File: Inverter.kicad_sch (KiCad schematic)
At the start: 44 parts, among them Q2 BSC022N04LSATMA1, Q3 BSC022N04LSATMA1, Q4 BSC022N04LSATMA1, Q5 BSC022N04LSATMA1, Q6 BSC022N04LSATMA1, Q7 BSC022N04LSATMA1, U4 TMC6140, U5 TSC2011, U6 TSC2011

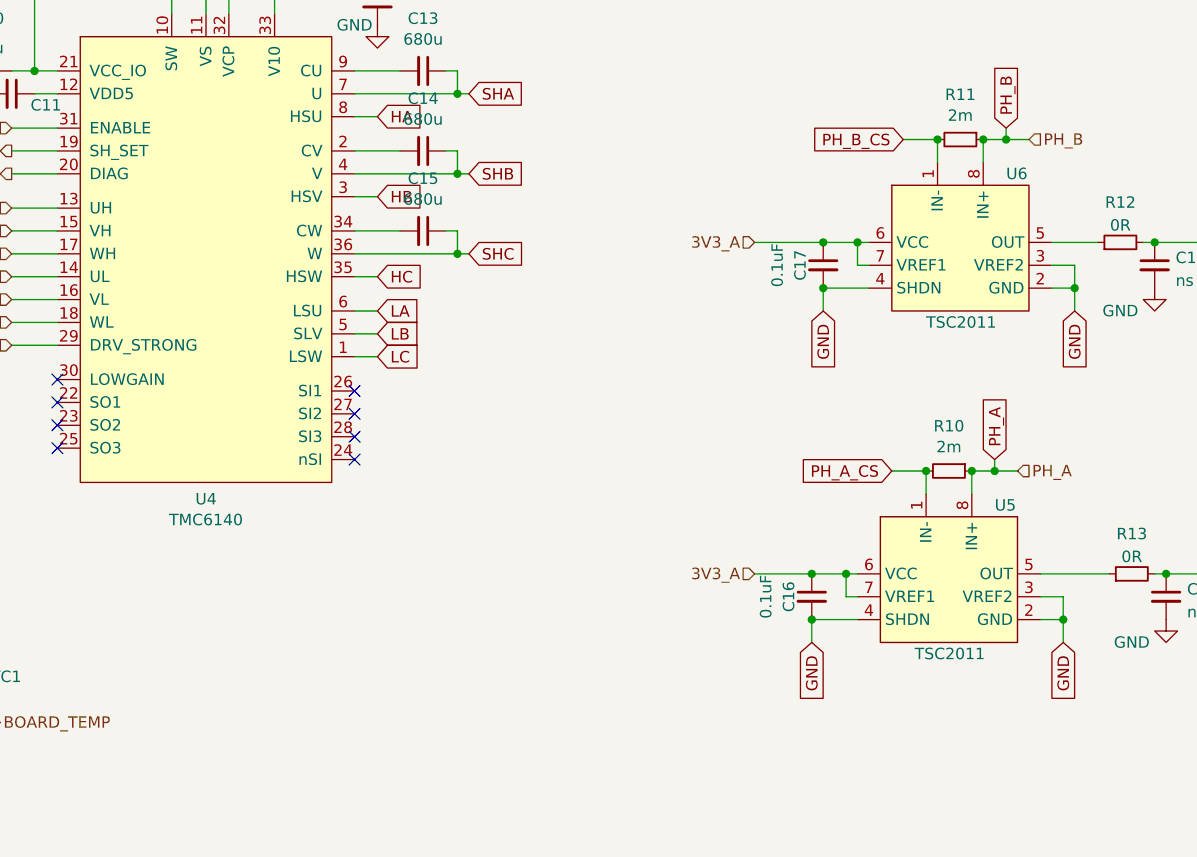
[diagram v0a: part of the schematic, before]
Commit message: added local symbol library
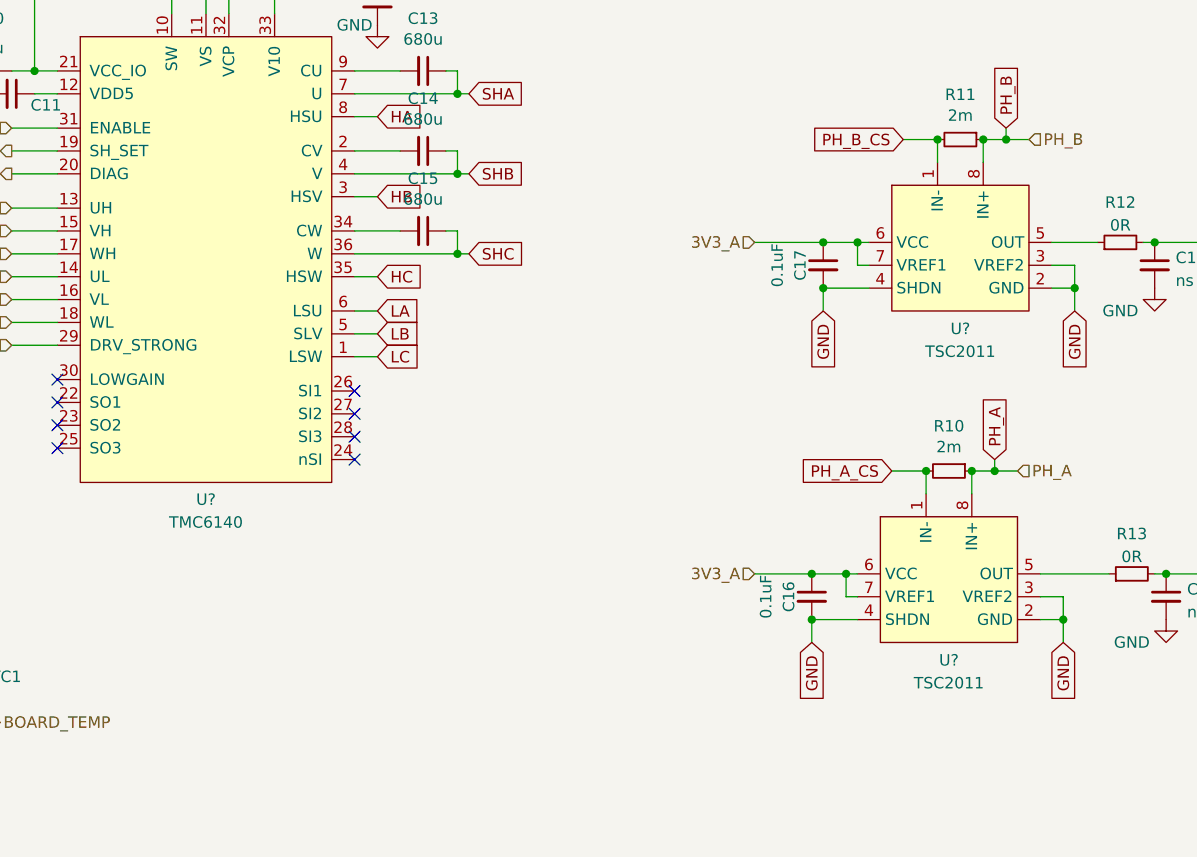
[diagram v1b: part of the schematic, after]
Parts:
- removed U4: TMC6140, symbol MyLibrary:TMC6140
- removed U5, U6: TSC2011, symbol Mylibrary:TSC2011
- added U? (x2): TSC2011, symbol MyLibrary_PMSM:TSC2011
- added U?: TMC6140, symbol MyLibrary_PMSM:TMC6140
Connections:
- net 3.3v: now also U?.21 (VCC_IO)
- net 3V3_A: now also U?.6 (VCC), U?.6 (VCC), U?.7 (VREF1), U?.7 (VREF1)
- net DIAG: now also U?.20 (DIAG)
- net DRV_STRONG: now also U?.29 (DRV_STRONG)
- net ENABLE: now also U?.31 (ENABLE)
- net GND: now also U?.2 (GND), U?.2 (GND), U?.3 (VREF2), U?.3 (VREF2), U?.4 (SHDN), U?.4 (SHDN)
- net HA: now also U?.8 (HSU)
- net HB: now also U?.3 (HSV)
- net HC: now also U?.35 (HSW)
- net LA: now also U?.6 (LSU)
- net LB: now also U?.5 (SLV)
- net LC: now also U?.1 (LSW)
- net PH_A: now also U?.8 (IN+)
- net PH_A_CS: now also U?.1 (IN-), U?.7 (U)
- net PH_B: now also U?.8 (IN+)
- net PH_B_CS: now also U?.1 (IN-), U?.4 (V)
- net PH_C: now also U?.36 (W)
- net PWM_HA: now also U?.13 (UH)
- net PWM_HB: now also U?.15 (VH)
- net PWM_HC: now also U?.17 (WH)
- net PWM_LA: now also U?.14 (UL)
- net PWM_LB: now also U?.16 (VL)
- net PWM_LC: now also U?.18 (WL)
- net SH_SET: now also U?.19 (SH_SET)
- net VDD: now also U?.11 (VS), U?.32 (VCP)
- net at C13.2: now also U?.9 (CU)
- net at C14.2: now also U?.2 (CV)
- net at C15.2: now also U?.34 (CW)
- net at 68u1.2: now also U?.10 (SW)
- net at C11.1: now also U?.12 (VDD5)
- net at C12.1: now also U?.33 (V10)
- net at R13.1: now also U?.5 (OUT)
- net at R12.1: now also U?.5 (OUT)

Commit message: Third commit
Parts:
- U4: renamed from U?; footprint (none) -> MyLibrary:TMC6140-LA
- gave numbers to parts that had none: 2
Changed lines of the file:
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@@
   (symbol (lib_id "MyLibrary_PMSM:TSC2011") (at 151.13 138.43 0) (unit 1)
     (in_bom yes) (on_board yes) (fields_autoplaced)
-    (property "Reference" "U?" (id 0) (at 151.13 150.5696 0))
+    (property "Reference" "U5" (id 0) (at 151.13 150.5696 0))
     (property "Value" "TSC2011" (id 1) (at 151.13 153.1065 0))
     (property "Footprint" "" (id 2) (at 151.13 138.43 0)
@@
   (symbol (lib_id "MyLibrary_PMSM:TMC6140") (at 68.58 105.41 0) (unit 1)
     (in_bom yes) (on_board yes) (fields_autoplaced)
-    (property "Reference" "U?" (id 0) (at 68.58 132.7134 0))
+    (property "Reference" "U4" (id 0) (at 68.58 132.7134 0))
     (property "Value" "TMC6140" (id 1) (at 68.58 135.2503 0))
-    (property "Footprint" "" (id 2) (at 83.82 93.98 0)
+    (property "Footprint" "MyLibrary:TMC6140-LA" (id 2) (at 83.82 93.98 0)
       (effects (font (size 1.27 1.27)) hide)
     )
@@
   (symbol (lib_id "MyLibrary_PMSM:TSC2011") (at 152.4 101.6 0) (unit 1)
     (in_bom yes) (on_board yes) (fields_autoplaced)
-    (property "Reference" "U?" (id 0) (at 152.4 113.7396 0))
+    (property "Reference" "U6" (id 0) (at 152.4 113.7396 0))
     (property "Value" "TSC2011" (id 1) (at 152.4 116.2765 0))
     (property "Footprint" "" (id 2) (at 152.4 101.6 0)

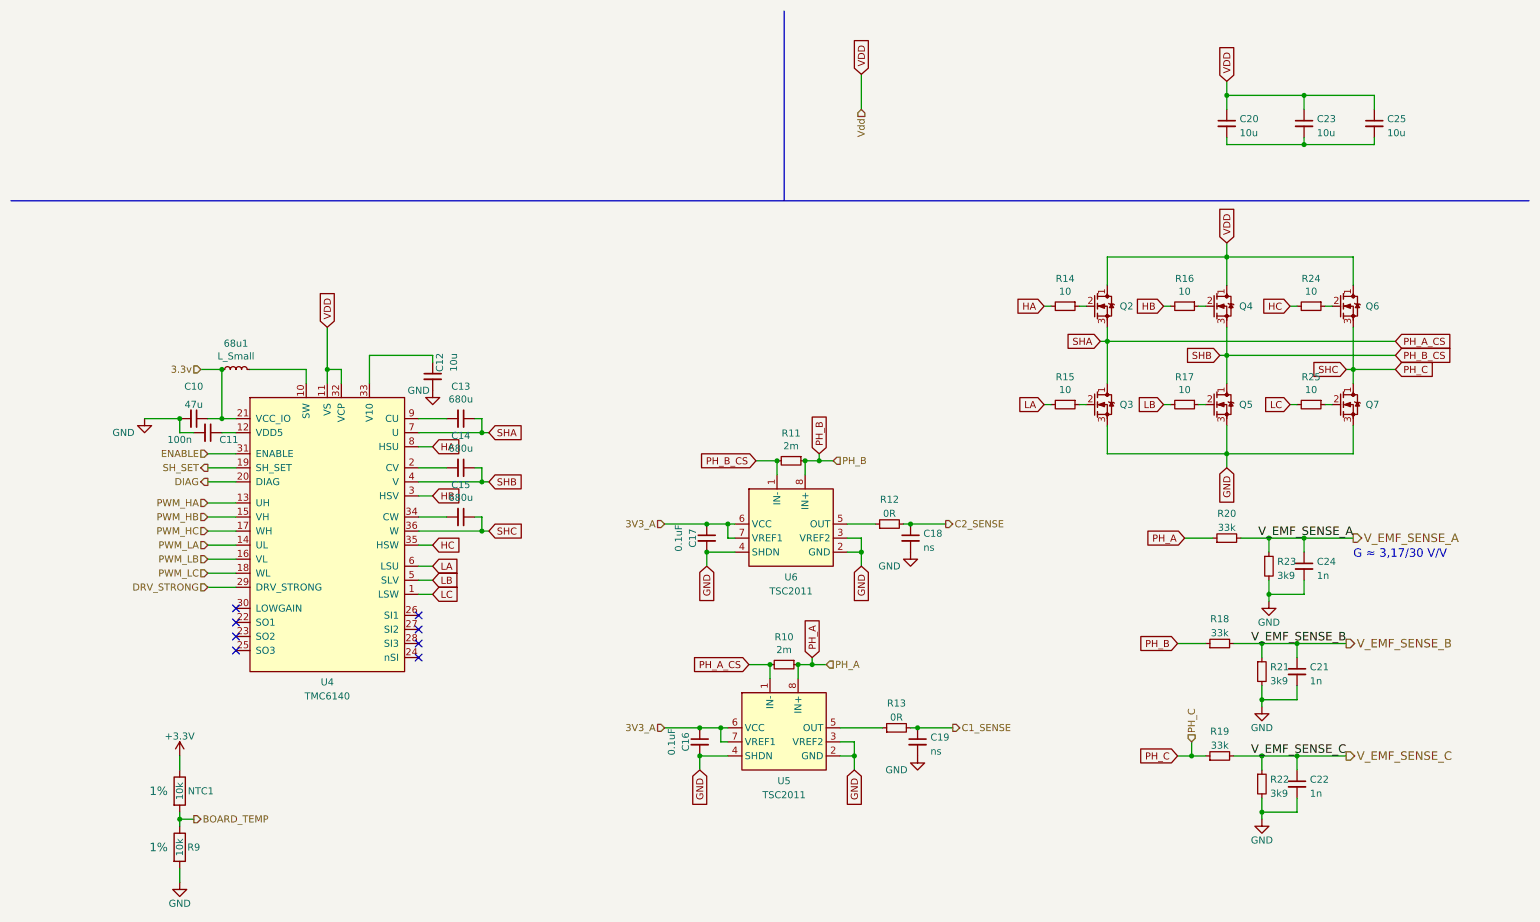
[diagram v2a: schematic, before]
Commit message: added footprints
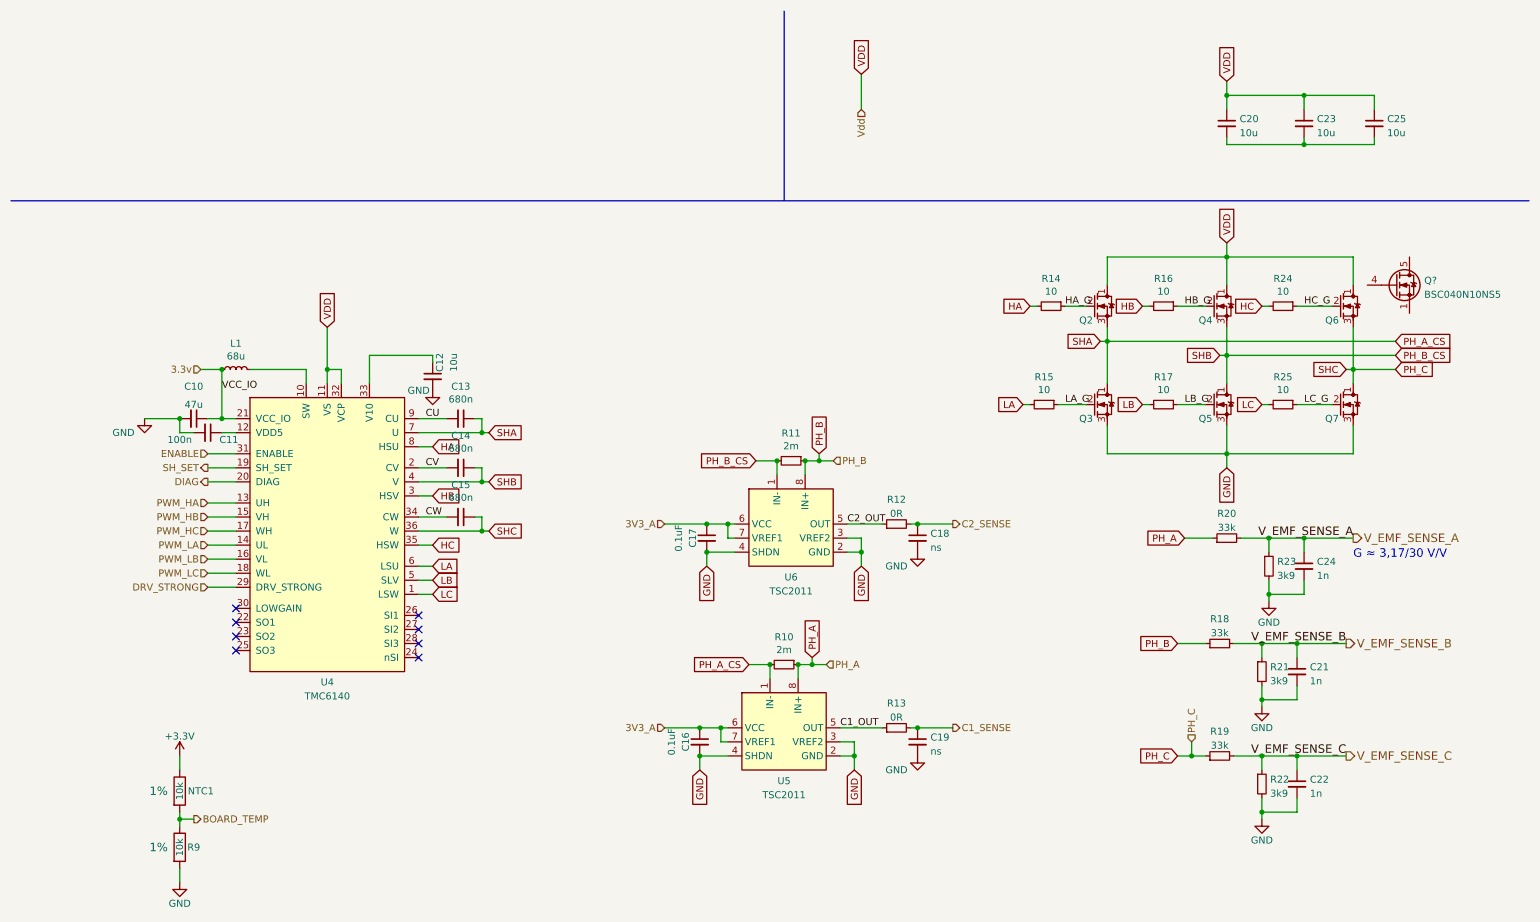
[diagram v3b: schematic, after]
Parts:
- added Q?: BSC040N10NS5, Package_TO_SOT_SMD:TDSON-8-1, symbol Transistor_FET:BSC040N10NS5
- C10: footprint (none) -> Capacitor_SMD:C_1206_3216Metric
- C11, C12, C18, C19, C20, C21, C22, C23, C24, C25: footprint (none) -> Capacitor_SMD:C_0603_1608Metric
- C13, C14, C15: value 680u -> 680n; footprint (none) -> Capacitor_SMD:C_0603_1608Metric
- L1: renamed from 68u1; value L_Small -> 68u; footprint (none) -> Inductor_SMD:L_Sunlord_MWSA0518_5.4x5.2mm
- Q2, Q3, Q4, Q5, Q6, Q7: footprint (none) -> MyLibrary:TDSON-8-6
- R10, R11: footprint (none) -> Resistor_SMD:R_2512_6332Metric
- R12, R13, R14, R15, R16, R17, R18, R19, R20, R21, R22, R23, R24, R25: footprint (none) -> Resistor_SMD:R_0603_1608Metric
- U5, U6: footprint (none) -> Package_SO:SOIC-8_3.9x4.9mm_P1.27mm
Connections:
- net HA_G: now reaches Q2.2 (G), R14.1
- net LA_G: now reaches Q3.2 (G), R15.1
- net HB_G: now reaches Q4.2 (G), R16.1
- net LB_G: now reaches Q5.2 (G), R17.1
- net HC_G: now reaches Q6.2 (G), R24.1
- net LC_G: now reaches Q7.2 (G), R25.1
- net CU: now reaches C13.2, U4.9 (CU)
- net CV: now reaches C14.2, U4.2 (CV)
- net CW: now reaches C15.2, U4.34 (CW)
- net C1_OUT: now reaches R13.1, U5.5 (OUT)
- net C2_OUT: now reaches R12.1, U6.5 (OUT)
- new net: Q?.1 (S), Q?.2 (S), Q?.3 (S)
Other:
- moved on the sheet: C18, R12, R14, R15, R16, R17, R24, R25

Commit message: fourth commit
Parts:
- Q2, Q3, Q4, Q5, Q6, Q7: footprint MyLibrary:TDSON-8-6 -> MyLibrary:TDSON-8-6_copy
- gave numbers to parts that had none: 1
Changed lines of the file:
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@@
       (effects (font (size 1.27 1.27)) (justify left) hide)
     )
-    (property "Footprint" "MyLibrary:TDSON-8-6" (id 2) (at 212.09 62.23 0)
+    (property "Footprint" "MyLibrary:TDSON-8-6_copy" (id 2) (at 212.09 62.23 0)
       (effects (font (size 1.27 1.27)) hide)
     )
@@
       (effects (font (size 1.27 1.27)) (justify left) hide)
     )
-    (property "Footprint" "MyLibrary:TDSON-8-6" (id 2) (at 212.09 80.01 0)
+    (property "Footprint" "MyLibrary:TDSON-8-6_copy" (id 2) (at 212.09 80.01 0)
       (effects (font (size 1.27 1.27)) hide)
     )
@@
       (effects (font (size 1.27 1.27)) (justify left) hide)
     )
-    (property "Footprint" "MyLibrary:TDSON-8-6" (id 2) (at 233.68 62.23 0)
+    (property "Footprint" "MyLibrary:TDSON-8-6_copy" (id 2) (at 233.68 62.23 0)
       (effects (font (size 1.27 1.27)) hide)
     )
@@
       (effects (font (size 1.27 1.27)) (justify left) hide)
     )
-    (property "Footprint" "MyLibrary:TDSON-8-6" (id 2) (at 233.68 80.01 0)
+    (property "Footprint" "MyLibrary:TDSON-8-6_copy" (id 2) (at 233.68 80.01 0)
       (effects (font (size 1.27 1.27)) hide)
     )
@@
       (effects (font (size 1.27 1.27)) (justify left) hide)
     )
-    (property "Footprint" "MyLibrary:TDSON-8-6" (id 2) (at 256.54 62.23 0)
+    (property "Footprint" "MyLibrary:TDSON-8-6_copy" (id 2) (at 256.54 62.23 0)
       (effects (font (size 1.27 1.27)) hide)
     )
@@
       (effects (font (size 1.27 1.27)) (justify left) hide)
     )
-    (property "Footprint" "MyLibrary:TDSON-8-6" (id 2) (at 256.54 80.01 0)
+    (property "Footprint" "MyLibrary:TDSON-8-6_copy" (id 2) (at 256.54 80.01 0)
       (effects (font (size 1.27 1.27)) hide)
     )
@@
   (symbol (lib_id "Transistor_FET:BSC040N10NS5") (at 261.62 60.96 0) (unit 1)
     (in_bom yes) (on_board yes) (fields_autoplaced)
-    (property "Reference" "Q?" (id 0) (at 266.827 60.1253 0)
-      (effects (font (size 1.27 1.27)) (justify left))
-    )
+    (property "Reference" "Q9" (id 0) (at 266.827 60.1253 0)
+      (effects (font (size 1.27 1.27)) (justify left))
+    )

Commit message: rev_0.1
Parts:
- removed Q9: BSC040N10NS5, Package_TO_SOT_SMD:TDSON-8-1, symbol Transistor_FET:BSC040N10NS5
- added C38: 22u, Capacitor_SMD:C_0603_1608Metric, symbol Device:C_Small
- C10: value 47u -> 22u; footprint Capacitor_SMD:C_1206_3216Metric -> Capacitor_SMD:C_0603_1608Metric
- L1: footprint Inductor_SMD:L_Sunlord_MWSA0518_5.4x5.2mm -> Inductor_SMD:L_1210_3225Metric
- NTC1: footprint Resistors_SMD:R_0603 -> Resistor_SMD:R_0603_1608Metric
- R9: footprint Resistors_SMD:R_0402 -> Resistor_SMD:R_0603_1608Metric
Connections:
- net 3.3v: now also C38.1
- net GND: now also C20.2, C23.2, C25.2, C38.2
- net HA: now also R16.2; no longer R14.2
- net HA_G: now also Q4.2 (G), R16.1; no longer Q2.2 (G), R14.1
- net HB: now also R24.2; no longer R16.2
- net HB_G: now also Q6.2 (G), R24.1; no longer Q4.2 (G), R16.1
- net HC: now also R14.2; no longer R24.2
- net HC_G: now also Q2.2 (G), R14.1; no longer Q6.2 (G), R24.1
- net LA: now also R17.2; no longer R15.2
- net LA_G: now also Q5.2 (G), R17.1; no longer Q3.2 (G), R15.1
- net LB: now also R25.2; no longer R17.2
- net LB_G: now also Q7.2 (G), R25.1; no longer Q5.2 (G), R17.1
- net LC: now also R15.2; no longer R25.2
- net LC_G: now also Q3.2 (G), R15.1; no longer Q7.2 (G), R25.1
- net PH_A: now also R11.1, U6.8 (IN+); no longer R10.1, R20.1, U5.8 (IN+)
- net PH_A_CS: now also Q4.3 (S), Q5.1 (D), R11.2, R19.1, U6.1 (IN-); no longer Q2.3 (S), Q3.1 (D), R10.2, U5.1 (IN-)
- net PH_B: now also C14.1, Q6.3 (S), Q7.1 (D), U4.4 (V); no longer R11.1, U6.8 (IN+)
- net PH_C: now also R10.1, U5.8 (IN+); no longer C15.1, Q6.3 (S), Q7.1 (D), R19.1, U4.36 (W)
- net V_EMF_SENSE_A: now also C22.1, R19.2, R22.1; no longer C24.1, R20.2, R23.1
- net V_EMF_SENSE_C: now also C24.1, R20.2, R23.1; no longer C22.1, R19.2, R22.1
- net SW: now reaches L1.2, U4.10 (SW)
- net V10: now reaches C12.1, U4.33 (V10)
- removed net PH_B_CS: C14.1, Q4.3 (S), Q5.1 (D), R11.2, U4.4 (V), U6.1 (IN-)
- new net PH_C_CS: C15.1, Q2.3 (S), Q3.1 (D), R10.2, R20.1, U4.36 (W), U5.1 (IN-)
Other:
- moved on the sheet: L1

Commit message: layout
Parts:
- added R35, R36, R6: 3k9, Resistor_SMD:R_0603_1608Metric, symbol Device:R_Small
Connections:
- net V_EMF_SENSE_A: now also R6.2; no longer R19.2, R22.1
- net V_EMF_SENSE_B: now also R35.2; no longer R18.2, R21.1
- net V_EMF_SENSE_C: now also R36.2; no longer R20.2, R23.1
- new net V_EMF_SENSE_A_NF: R19.2, R22.1, R6.1
- new net V_EMF_SENSE_B_NF: R18.2, R21.1, R35.1
- new net V_EMF_SENSE_C_NF: R20.2, R23.1, R36.1
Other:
- moved on the sheet: C21, C22, R18, R19, R20, R21, R22, R23

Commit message: before load switch
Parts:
- added D3, D7, D8: D_Zener_Small, Diode_SMD:D_SOD-123, symbol Device:D_Zener_Small
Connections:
- net GND: now also D3.2 (A), D7.2 (A), D8.2 (A)
- net V_EMF_SENSE_A: now also D3.1 (K)
- net V_EMF_SENSE_B: now also D7.1 (K)
- net V_EMF_SENSE_C: now also D8.1 (K)

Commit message: final
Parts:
- added C44, C45: 220n, Capacitor_SMD:C_0603_1608Metric, symbol Device:C_Small
- added C49, C50, C51: 1n, Capacitor_SMD:C_0603_1608Metric, symbol Device:C_Small
- added TP11, TP12, TP13, TP19, TP2, TP3, TP4, TP5, TP6, TP7, TP8, TP9: TestPoint, MyLibrary:TestPoint_1.0mm, symbol Connector:TestPoint
- added TP20, TP21, TP22, TP23, TP24, TP25, TP26, TP27: Testpoint, MyLibrary:TestPoint_1.0mm, symbol Connector:TestPoint
- C10, C38: Part (none) -> CL10A226MQ8NRNC
- C11: footprint Capacitor_SMD:C_0603_1608Metric -> Capacitor_SMD:C_0402_1005Metric; Part (none) -> CL05B104KA5NNNC
- C12: Part (none) -> CL21A106KOQNNNG
- C13, C14, C15: value 680n -> 1u; Part (none) -> CL10B105KA8NNNC
- C16, C17: value 0.1uF -> 100n; Part (none) -> CL05B104KA5NNNC
- C20, C23, C25: footprint Capacitor_SMD:C_0603_1608Metric -> Capacitor_SMD:C_1206_3216Metric; Part (none) -> CL31B106KBHNNNE
- C21, C22, C24: Part (none) -> CL10B102KB8NNNC
- D3, D7, D8: Part (none) -> MMSZ5231B-7-F
- L1: Part (none) -> CBC3225T680KR
- NTC1: Part (none) -> NCU18XH103F60RB
- Q2, Q3, Q4, Q5, Q6, Q7: Part (none) -> BSC022N04LSATMA1 ------
- R10, R11: Part (none) -> gia prese
- R14, R15, R16, R17, R24, R25: value 10 -> 2.2
- U4: Part (none) -> TMC6140 ---------
- U5, U6: Part (none) -> TSC2011 ----
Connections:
- net BOARD_TEMP: now also TP19.1
- net C1_SENSE: now also TP4.1
- net C2_SENSE: now also TP3.1
- net DIAG: now also TP22.1
- net ENABLE: now also TP20.1
- net GND: now also C44.2, C45.2, C49.2, C50.2, C51.2
- net HA: now also TP7.1
- net HB: now also TP9.1
- net HC: now also TP6.1
- net LA: now also TP8.1
- net LC: now also TP5.1
- net PH_A: now also R19.1
- net PH_A_CS: now also C50.1; no longer R19.1
- net PH_B: now also C51.1
- net PH_C: now also R20.1
- net PH_C_CS: now also C49.1; no longer R20.1
- net PWM_HA: now also TP23.1
- net PWM_HB: now also TP24.1
- net PWM_HC: now also TP25.1
- net PWM_LA: now also TP26.1
- net PWM_LB: now also TP27.1
- net SH_SET: now also TP21.1
- net VDD: now also C44.1, C45.1
- net V_EMF_SENSE_A: now also TP11.1
- net V_EMF_SENSE_B: now also TP12.1
- net V_EMF_SENSE_C: now also TP13.1
- net 3.3v renamed 3V3_TMC
- net 3V3_TMC: now also TP2.1
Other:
- moved on the sheet: C20, C23, C25, L1, Q2, Q3, Q4, Q5, Q6, Q7, R14, R15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
